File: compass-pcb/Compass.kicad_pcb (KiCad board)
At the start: 2 copper layers, 9 parts

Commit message: Polishing pcb design
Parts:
- moved GND 0.09 mm to (174.6, 83.8)
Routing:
- net GND: track 171.1 -> 137.7 mm, vias 5 -> 3
- net (no net): track 929.3 -> 962.6 mm, vias 53 -> 55
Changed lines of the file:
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@@
   )
   (footprint "Connector_Wire:SolderWire-0.5sqmm_1x01_D0.9mm_OD2.1mm" (layer "F.Cu")
-    (at 174.623939 83.729978)
+    (at 174.623939 83.82)
     (descr "Soldered wire connection, for a single 0.5 mm² wire, basic insulation, conductor diameter 0.9mm, outer diameter 2.1mm, size source Multi-Contact FLEXI-E 0.5 (https://ec.staubli.com/AcroFiles/Catalogues/TM_Cab-Main-11014119_(en)_hi.pdf), bend radius 3 times outer diameter, generated with kicad-footprint-generator")
     (tags "connector wire 0.5sqmm")
@@
     )
     (fp_text value " " (at 8.89 15.24 90) (layer "F.Fab")
-        (effects (font (size 1 1) (thickness 0.15)))
-    )
-    (fp_text user "Arduino Nano BLE Sense Rev2" (at 6.35 16.51 90) (layer "F.Fab")
         (effects (font (size 1 1) (thickness 0.15)))
     )
@@
   (segment (start 161.525445 115.563522) (end 165.521024 119.559101) (width 1.25) (layer "F.Cu") (net 0))
   (segment (start 115.805445 73.647654) (end 115.805445 70.182687) (width 1.25) (layer "F.Cu") (net 0))
+  (segment (start 118.188967 97.818533) (end 113.642359 102.365141) (width 1.25) (layer "F.Cu") (net 0))
   (segment (start 117.013324 95.278533) (end 128.505445 95.278533) (width 1.25) (layer "F.Cu") (net 0))
   (segment (start 125.092643 64.798533) (end 151.365445 64.798533) (width 1.25) (layer "F.Cu") (net 0))
@@
   (segment (start 131.216534 78.575209) (end 147.341357 78.575209) (width 1.25) (layer "F.Cu") (net 0))
   (segment (start 161.525445 78.981054) (end 161.525445 115.563522) (width 1.25) (layer "F.Cu") (net 0))
+  (segment (start 113.642359 102.365141) (end 113.642359 118.994041) (width 1.25) (layer "F.Cu") (net 0))
   (segment (start 166.605445 76.178973) (end 166.605445 101.855742) (width 1.25) (layer "F.Cu") (net 0))
   (segment (start 116.360985 118.969645) (end 116.289681 118.898341) (width 1.25) (layer "F.Cu") (net 0))
@@
   (segment (start 108.798645 77.476903) (end 108.820275 77.498533) (width 1.25) (layer "F.Cu") (net 0))
   (segment (start 179.347506 68.283233) (end 179.305445 68.325294) (width 1.25) (layer "F.Cu") (net 0))
-  (segment (start 172.092894 71.039311) (end 171.996358 71.135847) (width 1.25) (layer "F.Cu") (net 0))
   (segment (start 128.505445 107.978533) (end 131.045445 105.438533) (width 1.25) (layer "F.Cu") (net 0))
   (segment (start 118.345445 71.545731) (end 125.092643 64.798533) (width 1.25) (layer "F.Cu") (net 0))
@@
   (segment (start 149.882924 67.338533) (end 161.525445 78.981054) (width 1.25) (layer "F.Cu") (net 0))
   (segment (start 179.305445 94.8207) (end 182.258062 91.868083) (width 1.25) (layer "F.Cu") (net 0))
-  (segment (start 172.092894 68.275233) (end 172.092894 71.039311) (width 1.25) (layer "F.Cu") (net 0))
   (segment (start 111.954566 77.498533) (end 115.805445 73.647654) (width 1.25) (layer "F.Cu") (net 0))
   (segment (start 171.685445 102.898533) (end 174.280406 105.493494) (width 1.25) (layer "F.Cu") (net 0))
@@
   (segment (start 179.360406 100.413494) (end 184.975678 100.413494) (width 1.25) (layer "F.Cu") (net 0))
   (segment (start 171.996358 71.135847) (end 172.382759 71.135847) (width 1.25) (layer "F.Cu") (net 0))
+  (segment (start 128.505445 97.818533) (end 118.188967 97.818533) (width 1.25) (layer "F.Cu") (net 0))
   (via (at 172.092894 68.275233) (size 2) (drill 0.3) (layers "F.Cu" "B.Cu") (net 0))
   (via (at 179.347506 68.283233) (size 2) (drill 0.4) (layers "F.Cu" "B.Cu") (net 0))
@@
   (via (at 144.570556 81.187222) (size 2) (drill 0.4) (layers "F.Cu" "B.Cu") (net 0))
   (via (at 124.013168 110.518533) (size 2) (drill 0.3) (layers "F.Cu" "B.Cu") (net 0))
+  (via (at 113.642359 118.994041) (size 2) (drill 0.4) (layers "F.Cu" "B.Cu") (free) (net 0))
   (via (at 176.765445 123.218533) (size 2) (drill 0.4) (layers "F.Cu" "B.Cu") (net 0))
   (via (at 147.341357 81.187222) (size 2) (drill 0.4) (layers "F.Cu" "B.Cu") (net 0))
@@
   (via (at 174.632894 68.275233) (size 2) (drill 0.3) (layers "F.Cu" "B.Cu") (net 0))
   (via (at 171.685445 128.298533) (size 2) (drill 0.4) (layers "F.Cu" "B.Cu") (net 0))
+  (via (at 128.505445 97.818533) (size 2) (drill 0.3) (layers "F.Cu" "B.Cu") (free) (net 0))
   (via (at 108.798645 77.476903) (size 2) (drill 0.4) (layers "F.Cu" "B.Cu") (net 0))
   (via (at 184.993201 100.431017) (size 2) (drill 0.3) (layers "F.Cu" "B.Cu") (net 0))
@@
   (segment (start 179.492833 100.431017) (end 184.993201 100.431017) (width 1.25) (layer "B.Cu") (net 0))
   (segment (start 179.305445 100.358533) (end 179.250484 100.413494) (width 1.25) (layer "B.Cu") (net 0))
+  (segment (start 172.092894 71.039311) (end 171.996358 71.135847) (width 1.25) (layer "B.Cu") (net 0))
   (segment (start 171.685445 82.553161) (end 183.102759 71.135847) (width 1.25) (layer "B.Cu") (net 0))
   (segment (start 171.685445 100.358533) (end 161.525445 90.198533) (width 1.25) (layer "B.Cu") (net 0))
@@
   (segment (start 179.347506 68.283233) (end 173.322806 62.258533) (width 1.25) (layer "B.Cu") (net 0))
   (segment (start 161.525445 85.118533) (end 151.365445 74.958533) (width 1.25) (layer "B.Cu") (net 0))
+  (segment (start 172.092894 68.275233) (end 172.092894 71.039311) (width 1.25) (layer "B.Cu") (net 0))
   (segment (start 179.250484 100.413494) (end 171.685445 100.413494) (width 1.25) (layer "B.Cu") (net 0))
   (segment (start 183.102759 71.135847) (end 184.696358 71.135847) (width 1.25) (layer "B.Cu") (net 0))
@@
   (segment (start 158.985445 81.308533) (end 158.804244 81.127332) (width 1.25) (layer "F.Cu") (net 1))
   (segment (start 158.985445 125.758533) (end 165.127278 131.900366) (width 1.25) (layer "F.Cu") (net 1))
-  (segment (start 113.751738 118.95987) (end 113.761513 118.969645) (width 1.25) (layer "F.Cu") (net 1))
   (segment (start 149.967503 81.127332) (end 149.927814 81.167021) (width 1.25) (layer "F.Cu") (net 1))
   (segment (start 169.145445 131.900366) (end 169.145445 128.298533) (width 1.25) (layer "F.Cu") (net 1))
   (segment (start 124.013168 77.498533) (end 125.965445 77.498533) (width 1.25) (layer "F.Cu") (net 1))
   (segment (start 158.985445 81.308533) (end 158.985445 125.758533) (width 1.25) (layer "F.Cu") (net 1))
-  (segment (start 113.617837 118.898341) (end 113.617837 102.546141) (width 1.25) (layer "F.Cu") (net 1))
   (segment (start 174.638062 101.433113) (end 176.28909 103.084141) (width 1.25) (layer "F.Cu") (net 1))
   (segment (start 174.623939 83.729978) (end 174.638062 83.744101) (width 1.25) (layer "F.Cu") (net 1))
@@
   (segment (start 125.965445 77.498533) (end 128.505445 74.958533) (width 1.25) (layer "F.Cu") (net 1))
   (segment (start 174.638062 83.744101) (end 174.638062 101.433113) (width 1.25) (layer "F.Cu") (net 1))
-  (segment (start 113.689141 118.969645) (end 113.617837 118.898341) (width 1.25) (layer "F.Cu") (net 1))
-  (segment (start 118.345445 97.818533) (end 128.505445 97.818533) (width 1.25) (layer "F.Cu") (net 1))
   (segment (start 152.635445 74.958533) (end 158.985445 81.308533) (width 1.25) (layer "F.Cu") (net 1))
   (segment (start 184.993201 102.971017) (end 185.048162 102.916056) (width 1.25) (layer "F.Cu") (net 1))
   (segment (start 184.972459 102.991759) (end 184.993201 102.971017) (width 1.25) (layer "F.Cu") (net 1))
   (segment (start 165.127278 131.900366) (end 169.145445 131.900366) (width 1.25) (layer "F.Cu") (net 1))
-  (segment (start 113.689141 118.897273) (end 113.689141 118.897273) (width 1.25) (layer "F.Cu") (net 1))
   (segment (start 128.505445 74.958533) (end 152.635445 74.958533) (width 1.25) (layer "F.Cu") (net 1))
-  (segment (start 113.617837 102.546141) (end 118.345445 97.818533) (width 1.25) (layer "F.Cu") (net 1))
   (segment (start 184.993201 102.971017) (end 185.097489 103.075305) (width 1.25) (layer "F.Cu") (net 1))
-  (segment (start 113.761513 118.969645) (end 113.689141 118.969645) (width 1.25) (layer "F.Cu") (net 1))
   (via (at 169.145445 128.298533) (size 2) (drill 0.4) (layers "F.Cu" "B.Cu") (net 1))
   (via (at 184.993201 102.971017) (size 2) (drill 0.3) (layers "F.Cu" "B.Cu") (net 1))
-  (via (at 113.689141 118.969645) (size 2) (drill 0.4) (layers "F.Cu" "B.Cu") (net 1))
-  (via (at 128.505445 97.818533) (size 2) (drill 0.3) (layers "F.Cu" "B.Cu") (net 1))
   (via (at 124.013168 77.498533) (size 2) (drill 0.4) (layers "F.Cu" "B.Cu") (net 1))
   (segment (start 184.883296 102.861112) (end 184.993201 102.971017) (width 1.25) (layer "B.Cu") (net 1))

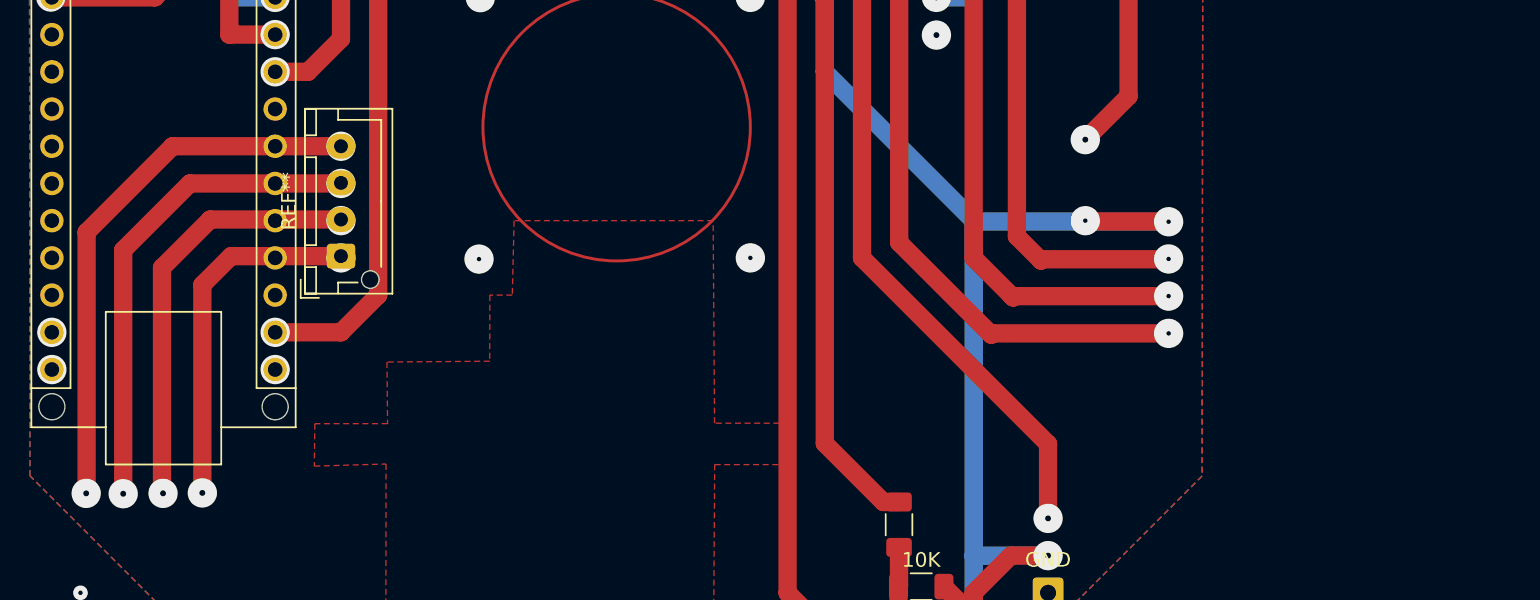
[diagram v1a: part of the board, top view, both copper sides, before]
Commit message: fixing USB contacts to be one-sided
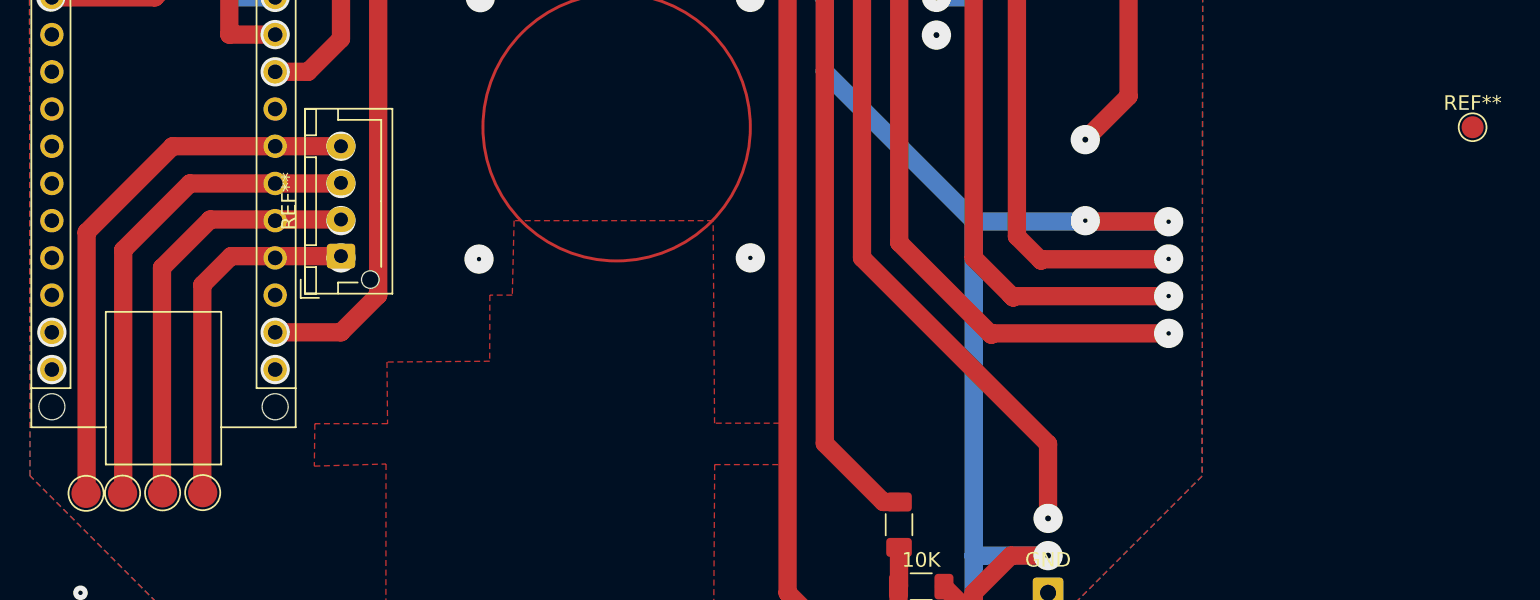
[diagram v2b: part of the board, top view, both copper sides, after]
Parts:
- added REF**: , TestPoint:TestPoint_Pad_D2.0mm, F.Cu at (113.6, 119.0)
- added REF**: TestPoint_Pad_D1.5mm, TestPoint:TestPoint_Pad_D1.5mm, F.Cu at (205.7, 94.0)
- added REF**: , TestPoint:TestPoint_Pad_D2.0mm, F.Cu at (111.1, 119.0)
- added REF**: , TestPoint:TestPoint_Pad_D2.0mm, F.Cu at (116.3, 118.9)
- added REF**: , TestPoint:TestPoint_Pad_D2.0mm, F.Cu at (119.1, 118.9)
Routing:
- net (no net): vias 55 -> 51
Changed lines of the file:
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@@
     )
+  )
+  (footprint "TestPoint:TestPoint_Pad_D2.0mm" (layer "F.Cu")
+    (at 113.599676 118.951239)
+    (descr "SMD pad as test Point, diameter 2.0mm")
+    (tags "test point SMD pad")
+    (attr exclude_from_pos_files exclude_from_bom)
+    (fp_text reference "REF**" (at 0 -1.998) (layer "F.SilkS") hide
+        (effects (font (size 1 1) (thickness 0.15)))
+    )
+    (fp_text value " " (at 0 2.05) (layer "F.Fab")
+        (effects (font (size 1 1) (thickness 0.15)))
+    )
+    (fp_circle (center 0 0) (end 0 1.2)
+      (stroke (width 0.12) (type solid)) (fill none) (layer "F.SilkS"))
+    (fp_circle (center 0 0) (end 1.5 0)
+      (stroke (width 0.05) (type solid)) (fill none) (layer "F.CrtYd"))
+    (pad "1" smd circle (at 0 0) (size 2 2) (layers "F.Cu" "F.Mask"))
+    (pad "1" smd circle (at 0 0) (size 2 2) (layers "F.Cu" "F.Mask"))
   )
   (footprint "Resistor_SMD:R_1206_3216Metric_Pad1.30x1.75mm_HandSolder" (layer "F.Cu")
@@
       (rotate (xyz 0 0 0))
     )
+  )
+  (footprint "TestPoint:TestPoint_Pad_D1.5mm" (layer "F.Cu")
+    (at 205.74 93.98)
+    (descr "SMD pad as test Point, diameter 1.5mm")
+    (tags "test point SMD pad")
+    (attr exclude_from_pos_files exclude_from_bom)
+    (fp_text reference "REF**" (at 0 -1.648) (layer "F.SilkS")
+        (effects (font (size 1 1) (thickness 0.15)))
+    )
+    (fp_text value "TestPoint_Pad_D1.5mm" (at 0 1.75) (layer "F.Fab")
+        (effects (font (size 1 1) (thickness 0.15)))
+    )
+    (fp_text user "${REFERENCE}" (at 0 -1.65) (layer "F.Fab")
+        (effects (font (size 1 1) (thickness 0.15)))
+    )
+    (fp_circle (center 0 0) (end 0 0.95)
+      (stroke (width 0.12) (type solid)) (fill none) (layer "F.SilkS"))
+    (fp_circle (center 0 0) (end 1.25 0)
+      (stroke (width 0.05) (type solid)) (fill none) (layer "F.CrtYd"))
+    (pad "1" smd circle (at 0 0) (size 1.5 1.5) (layers "F.Cu" "F.Mask"))
+  )
+  (footprint "TestPoint:TestPoint_Pad_D2.0mm" (layer "F.Cu")
+    (at 111.106514 118.967119)
+    (descr "SMD pad as test Point, diameter 2.0mm")
+    (tags "test point SMD pad")
+    (attr exclude_from_pos_files exclude_from_bom)
+    (fp_text reference "REF**" (at 0 -1.998) (layer "F.SilkS") hide
+        (effects (font (size 1 1) (thickness 0.15)))
+    )
+    (fp_text value " " (at 0 2.05) (layer "F.Fab")
+        (effects (font (size 1 1) (thickness 0.15)))
+    )
+    (fp_text user " " (at 0 -2) (layer "F.Fab")
+        (effects (font (size 1 1) (thickness 0.15)))
+    )
+    (fp_circle (center 0 0) (end 0 1.2)
+      (stroke (width 0.12) (type solid)) (fill none) (layer "F.SilkS"))
+    (fp_circle (center 0 0) (end 1.5 0)
+      (stroke (width 0.05) (type solid)) (fill none) (layer "F.CrtYd"))
+    (pad "1" smd circle (at 0 0) (size 2 2) (layers "F.Cu" "F.Mask"))
+    (pad "1" smd circle (at 0 0) (size 2 2) (layers "F.Cu" "F.Mask"))
   )
   (footprint "Resistor_SMD:R_1206_3216Metric_Pad1.30x1.75mm_HandSolder" (layer "F.Cu")
@@
     )
   )
+  (footprint "TestPoint:TestPoint_Pad_D2.0mm" (layer "F.Cu")
+    (at 116.331037 118.935359)
+    (descr "SMD pad as test Point, diameter 2.0mm")
+    (tags "test point SMD pad")
+    (attr exclude_from_pos_files exclude_from_bom)
+    (fp_text reference "REF**" (at 0 -1.998) (layer "F.SilkS") hide
+        (effects (font (size 1 1) (thickness 0.15)))
+    )
+    (fp_text value " " (at 0 2.05) (layer "F.Fab")
+        (effects (font (size 1 1) (thickness 0.15)))
+    )
+    (fp_circle (center 0 0) (end 0 1.2)
+      (stroke (width 0.12) (type solid)) (fill none) (layer "F.SilkS"))
+    (fp_circle (center 0 0) (end 1.5 0)
+      (stroke (width 0.05) (type solid)) (fill none) (layer "F.CrtYd"))
+    (pad "1" smd circle (at 0 0) (size 2 2) (layers "F.Cu" "F.Mask"))
+    (pad "1" smd circle (at 0 0) (size 2 2) (layers "F.Cu" "F.Mask"))
+  )
   (footprint "Connector_Wire:SolderWire-0.5sqmm_1x01_D0.9mm_OD2.1mm" (layer "F.Cu")
     (at 149.927814 81.167021)
@@
       (rotate (xyz 0 0 0))
     )
+  )
+  (footprint "TestPoint:TestPoint_Pad_D2.0mm" (layer "F.Cu")
+    (at 119.067837 118.919124)
+    (descr "SMD pad as test Point, diameter 2.0mm")
+    (tags "test point SMD pad")
+    (attr exclude_from_pos_files exclude_from_bom)
+    (fp_text reference "REF**" (at 0 -1.998) (layer "F.SilkS") hide
+        (effects (font (size 1 1) (thickness 0.15)))
+    )
+    (fp_text value " " (at 0 2.05) (layer "F.Fab")
+        (effects (font (size 1 1) (thickness 0.15)))
+    )
+    (fp_circle (center 0 0) (end 0 1.2)
+      (stroke (width 0.12) (type solid)) (fill none) (layer "F.SilkS"))
+    (fp_circle (center 0 0) (end 1.5 0)
+      (stroke (width 0.05) (type solid)) (fill none) (layer "F.CrtYd"))
+    (pad "1" smd circle (at 0 0) (size 2 2) (layers "F.Cu" "F.Mask"))
+    (pad "1" smd circle (at 0 0) (size 2 2) (layers "F.Cu" "F.Mask"))
   )
   (gr_circle (center 147.32 93.98) (end 156.445445 93.98)
@@
   (via (at 108.798645 74.904016) (size 2) (drill 0.4) (layers "F.Cu" "B.Cu") (net 0))
   (via (at 124.013168 87.658533) (size 2) (drill 0.4) (layers "F.Cu" "B.Cu") (net 0))
-  (via (at 119.0428 118.939968) (size 2) (drill 0.4) (layers "F.Cu" "B.Cu") (free) (net 0))
-  (via (at 116.360985 118.969645) (size 2) (drill 0.4) (layers "F.Cu" "B.Cu") (net 0))
   (via (at 108.185445 133.378533) (size 1) (drill 0.3) (layers "F.Cu" "B.Cu") (net 0))
   (via (at 108.699687 85.096606) (size 2) (drill 0.4) (layers "F.Cu" "B.Cu") (net 0))
@@
   (via (at 144.570556 81.187222) (size 2) (drill 0.4) (layers "F.Cu" "B.Cu") (net 0))
   (via (at 124.013168 110.518533) (size 2) (drill 0.3) (layers "F.Cu" "B.Cu") (net 0))
-  (via (at 113.642359 118.994041) (size 2) (drill 0.4) (layers "F.Cu" "B.Cu") (free) (net 0))
   (via (at 176.765445 123.218533) (size 2) (drill 0.4) (layers "F.Cu" "B.Cu") (net 0))
   (via (at 147.341357 81.187222) (size 2) (drill 0.4) (layers "F.Cu" "B.Cu") (net 0))
   (via (at 137.925772 102.979598) (size 2) (drill 0.3) (layers "F.Cu" "B.Cu") (net 0))
-  (via (at 111.116254 118.969645) (size 2) (drill 0.4) (layers "F.Cu" "B.Cu") (net 0))
   (via (at 181.845445 59.718533) (size 1) (drill 0.3) (layers "F.Cu" "B.Cu") (net 0))
   (via (at 176.765445 120.678533) (size 2) (drill 0.4) (layers "F.Cu" "B.Cu") (net 0))
